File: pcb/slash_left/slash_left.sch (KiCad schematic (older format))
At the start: 76 parts

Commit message: pcb: slash: Matrix schematic
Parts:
- added D?: D_Small, symbol Device:D_Small
- added SW?: SW_Push_45deg, symbol Switch:SW_Push_45deg
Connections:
- net COL11: now also SW?.2
- net ROW0: now also D?.1 (K)
- new net: D?.2 (A), SW?.1
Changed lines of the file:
@@
 	5250 4600 6150 4600
 Wire Wire Line
-	6800 3650 6800 4900
+	6800 3650 6800 4200
 Wire Wire Line
-	6150 4600 7000 4600
+	6150 4600 6600 4600
+$Comp
+L Switch:SW_Push_45deg SW?
+U 1 1 61596B0E
+P 6700 4300
+F 0 "SW?" V 6600 4350 50  0000 R CNN
+F 1 "SW_Push_45deg" V 6655 4156 50  0001 R CNN
+F 2 "" H 6700 4300 50  0001 C CNN
+F 3 "~" H 6700 4300 50  0001 C CNN
+	1    6700 4300
+	0    -1   -1   0
+$EndComp
+$Comp
+L Device:D_Small D?
+U 1 1 615972C0
+P 6600 4500
+F 0 "D?" V 6600 4430 50  0000 R CNN
+F 1 "D_Small" V 6555 4430 50  0001 R CNN
+F 2 "" V 6600 4500 50  0001 C CNN
+F 3 "~" V 6600 4500 50  0001 C CNN
+	1    6600 4500
+	0    -1   -1   0
+$EndComp
+Connection ~ 6600 4600
+Wire Wire Line
+	6600 4600 7000 4600
+Connection ~ 6800 4200
+Wire Wire Line
+	6800 4200 6800 4900
 $EndSCHEMATC

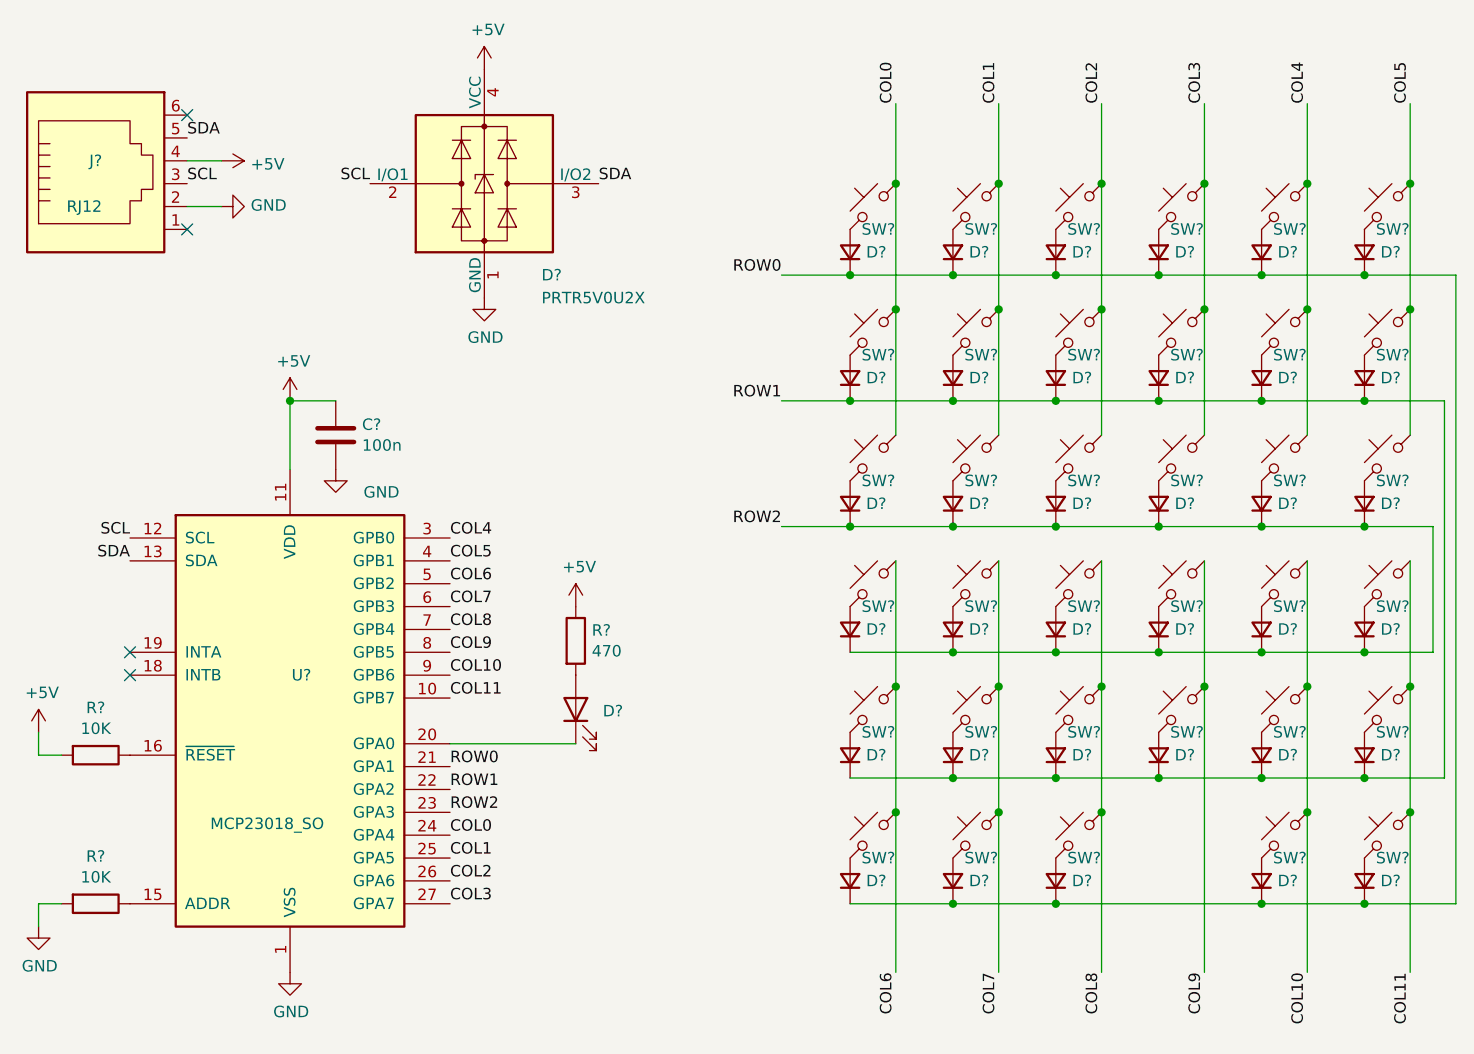
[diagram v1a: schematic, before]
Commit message: pcb: slash: left: Assign footprints
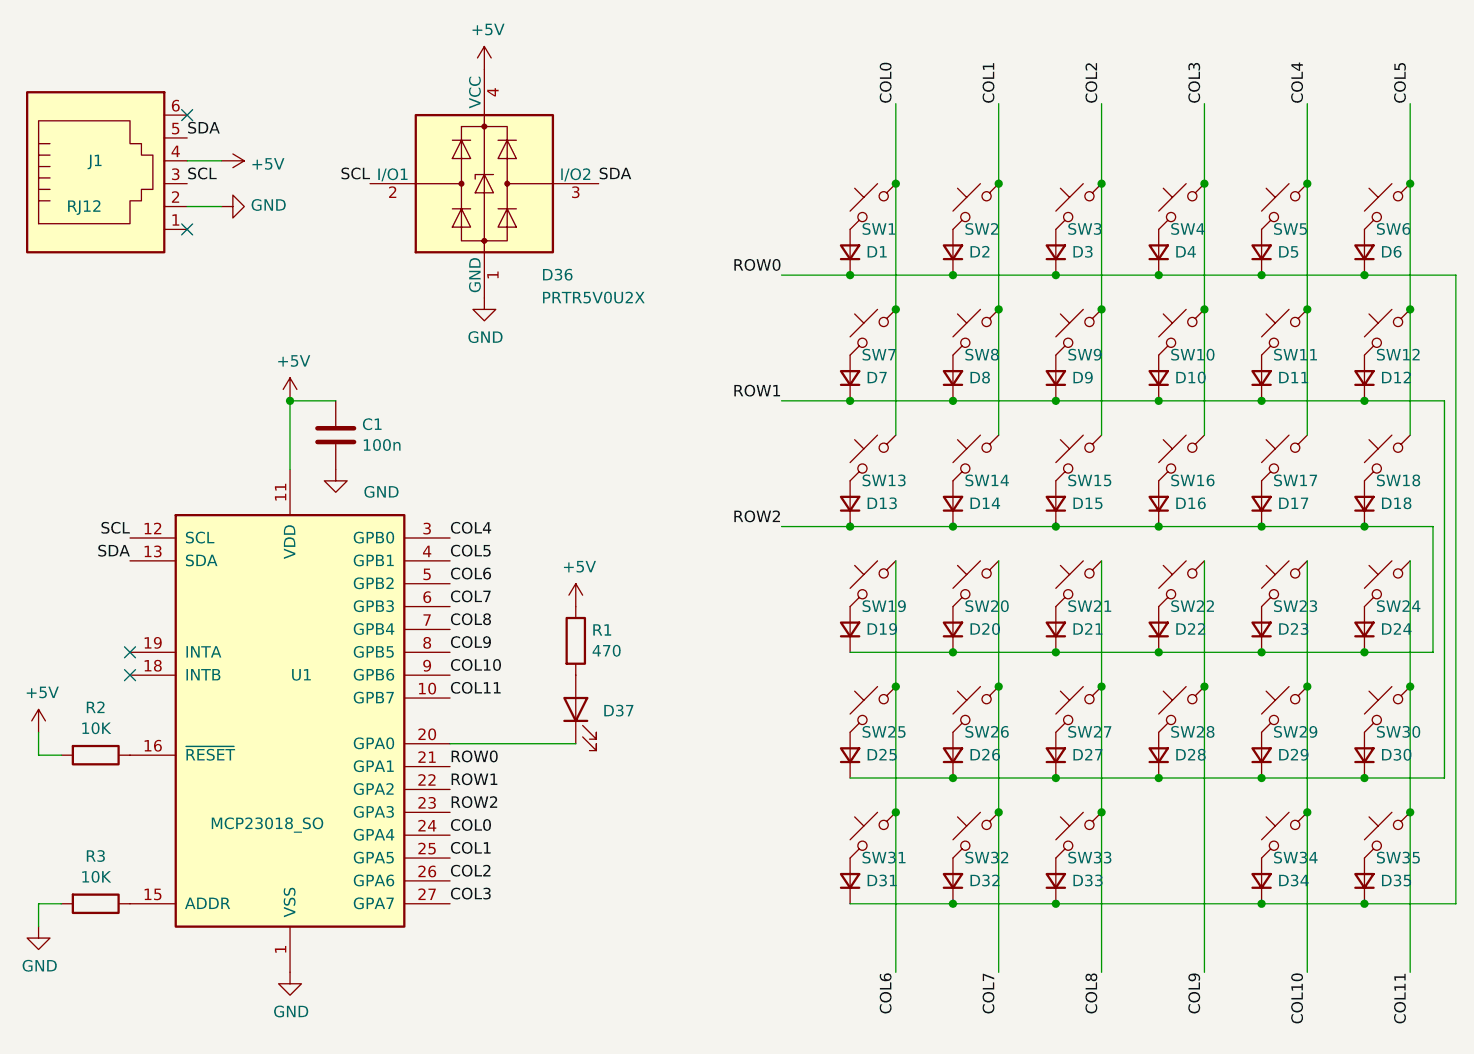
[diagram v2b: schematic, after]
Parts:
- C1: renamed from C?; footprint (none) -> Capacitor_SMD:C_0805_2012Metric_Pad1.18x1.45mm_HandSolder
- D1, D10, D11, D12, D13, D14, D15, D16, D17, D18, D19, D2, D20, D21, D22, D23, D24, D25, D26, D27, D28, D29, D3, D30, D31, D32, D33, D34, D35, D4, D5, D6, D7, D8, D9: renamed from D?; footprint (none) -> Diode_SMD:D_SOD-123
- D37: renamed from D?; footprint (none) -> LED_SMD:LED_0805_2012Metric_Pad1.15x1.40mm_HandSolder
- J1: renamed from J?; footprint (none) -> local_footprint:RJ12_Custom1
- R1, R2, R3: renamed from R?; footprint (none) -> Resistor_SMD:R_0805_2012Metric_Pad1.20x1.40mm_HandSolder
- SW1, SW10, SW11, SW12, SW13, SW14, SW15, SW16, SW17, SW18, SW19, SW2, SW20, SW21, SW22, SW23, SW24, SW25, SW26, SW27, SW28, SW29, SW3, SW30, SW31, SW32, SW33, SW34, SW35, SW4, SW5, SW6, SW7, SW8, SW9: renamed from SW?; footprint (none) -> keyswitches:Kailh_socket_MX
- gave numbers to parts that had none: 2

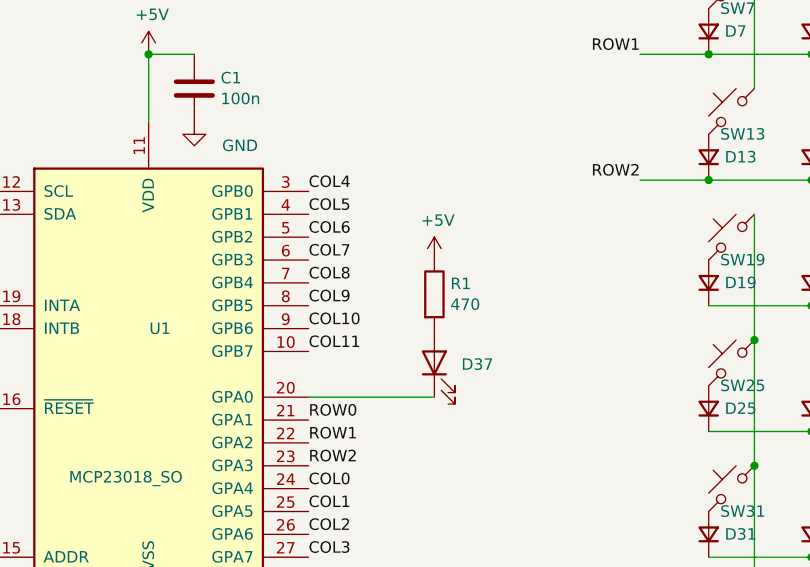
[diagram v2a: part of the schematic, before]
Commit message: pcb: slash: left: Routing
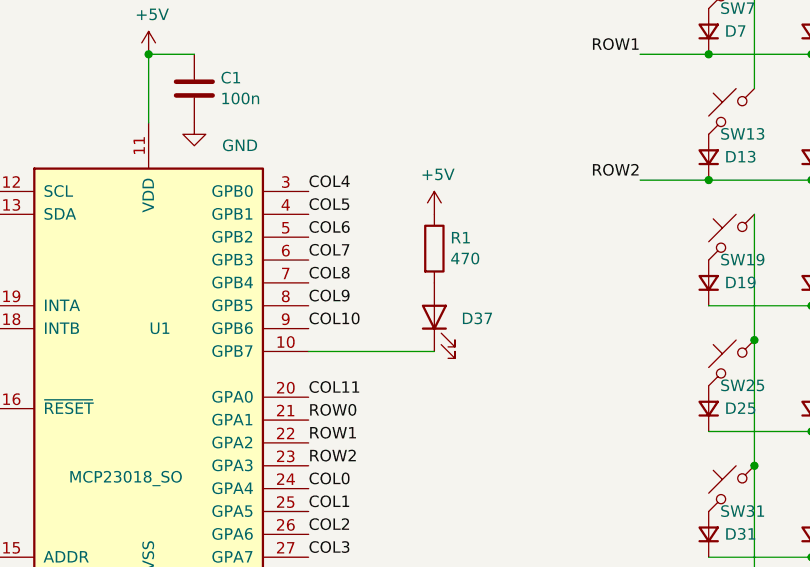
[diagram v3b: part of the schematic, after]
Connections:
- net COL11: now also U1.20 (GPA0); no longer U1.10 (GPB7)
- net at D37.1 (K): now also U1.10 (GPB7); no longer U1.20 (GPA0)
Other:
- moved on the sheet: D37, R1
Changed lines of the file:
@@
 L Device:LED D37
 U 1 1 6152B15D
-P 3150 3750
-F 0 "D37" V 3143 3632 50  0000 R CNN
-F 1 "LED" V 3098 3632 50  0001 R CNN
-F 2 "LED_SMD:LED_0805_2012Metric_Pad1.15x1.40mm_HandSolder" H 3150 3750 50  0001 C CNN
-F 3 "~" H 3150 3750 50  0001 C CNN
-	1    3150 3750
+P 3150 3550
+F 0 "D37" V 3143 3432 50  0000 R CNN
+F 1 "LED" V 3098 3432 50  0001 R CNN
+F 2 "LED_SMD:LED_0805_2012Metric_Pad1.15x1.40mm_HandSolder" H 3150 3550 50  0001 C CNN
+F 3 "~" H 3150 3550 50  0001 C CNN
+	1    3150 3550
 	0    -1   -1   0
 $EndComp
@@
 L Device:R R1
 U 1 1 6152D409
-P 3150 3450
-F 0 "R1" H 3220 3496 50  0000 L CNN
-F 1 "470" H 3220 3405 50  0000 L CNN
-F 2 "Resistor_SMD:R_0805_2012Metric_Pad1.20x1.40mm_HandSolder" V 3080 3450 50  0001 C CNN
-F 3 "~" H 3150 3450 50  0001 C CNN
-	1    3150 3450
+P 3150 3250
+F 0 "R1" H 3220 3296 50  0000 L CNN
+F 1 "470" H 3220 3205 50  0000 L CNN
+F 2 "Resistor_SMD:R_0805_2012Metric_Pad1.20x1.40mm_HandSolder" V 3080 3250 50  0001 C CNN
+F 3 "~" H 3150 3250 50  0001 C CNN
+	1    3150 3250
 	1    0    0    -1
 $EndComp
@@
 L power:+5V #PWR07
 U 1 1 6152E45E
-P 3150 3300
-F 0 "#PWR07" H 3150 3150 50  0001 C CNN
-F 1 "+5V" H 3165 3473 50  0000 C CNN
-F 2 "" H 3150 3300 50  0001 C CNN
-F 3 "" H 3150 3300 50  0001 C CNN
-	1    3150 3300
+P 3150 3100
+F 0 "#PWR07" H 3150 2950 50  0001 C CNN
+F 1 "+5V" H 3165 3273 50  0000 C CNN
+F 2 "" H 3150 3100 50  0001 C CNN
+F 3 "" H 3150 3100 50  0001 C CNN
+	1    3150 3100
 	1    0    0    -1
 $EndComp
 Wire Wire Line
-	3150 3900 2600 3900
+	3150 3700 2600 3700
 Text Label 2600 4000 0    50   ~ 0
 ROW0
@@
 Text Label 2600 3600 0    50   ~ 0
 COL10
-Text Label 2600 3700 0    50   ~ 0
+Text Label 2600 3900 0    50   ~ 0
 COL11
 Wire Wire Line

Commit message: pcb: slash: left: finish
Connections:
- net COL0: now also U1.6 (GPB3); no longer U1.24 (GPA4)
- net COL1: now also U1.7 (GPB4); no longer U1.25 (GPA5)
- net COL10: now also U1.22 (GPA2); no longer U1.9 (GPB6)
- net COL11: now also U1.21 (GPA1); no longer U1.20 (GPA0)
- net COL2: now also U1.8 (GPB5); no longer U1.26 (GPA6)
- net COL3: now also U1.9 (GPB6); no longer U1.27 (GPA7)
- net COL4: now also U1.27 (GPA7); no longer U1.3 (GPB0)
- net COL5: now also U1.20 (GPA0); no longer U1.4 (GPB1)
- net COL6: now also U1.26 (GPA6); no longer U1.5 (GPB2)
- net COL7: now also U1.25 (GPA5); no longer U1.6 (GPB3)
- net COL8: now also U1.24 (GPA4); no longer U1.7 (GPB4)
- net COL9: now also U1.23 (GPA3); no longer U1.8 (GPB5)
- net ROW0: now also U1.3 (GPB0); no longer U1.21 (GPA1)
- net ROW1: now also U1.4 (GPB1); no longer U1.22 (GPA2)
- net ROW2: now also U1.5 (GPB2); no longer U1.23 (GPA3)
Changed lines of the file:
@@
 Wire Wire Line
 	3150 3700 2600 3700
+Text Label 2600 3000 0    50   ~ 0
+ROW0
+Text Label 2600 3100 0    50   ~ 0
+ROW1
+Text Label 2600 3200 0    50   ~ 0
+ROW2
+Text Label 2600 3300 0    50   ~ 0
+COL0
+Text Label 2600 3400 0    50   ~ 0
+COL1
+Text Label 2600 3500 0    50   ~ 0
+COL2
+Text Label 2600 3600 0    50   ~ 0
+COL3
+Text Label 2600 4600 0    50   ~ 0
+COL4
+Text Label 2600 3900 0    50   ~ 0
+COL5
+Text Label 2600 4500 0    50   ~ 0
+COL6
+Text Label 2600 4400 0    50   ~ 0
+COL7
+Text Label 2600 4300 0    50   ~ 0
+COL8
+Text Label 2600 4200 0    50   ~ 0
+COL9
+Text Label 2600 4100 0    50   ~ 0
+COL10
 Text Label 2600 4000 0    50   ~ 0
-ROW0
-Text Label 2600 4100 0    50   ~ 0
-ROW1
-Text Label 2600 4200 0    50   ~ 0
-ROW2
-Text Label 2600 4300 0    50   ~ 0
-COL0
-Text Label 2600 4400 0    50   ~ 0
-COL1
-Text Label 2600 4500 0    50   ~ 0
-COL2
-Text Label 2600 4600 0    50   ~ 0
-COL3
-Text Label 2600 3000 0    50   ~ 0
-COL4
-Text Label 2600 3100 0    50   ~ 0
-COL5
-Text Label 2600 3200 0    50   ~ 0
-COL6
-Text Label 2600 3300 0    50   ~ 0
-COL7
-Text Label 2600 3400 0    50   ~ 0
-COL8
-Text Label 2600 3500 0    50   ~ 0
-COL9
-Text Label 2600 3600 0    50   ~ 0
-COL10
-Text Label 2600 3900 0    50   ~ 0
 COL11
 Wire Wire Line

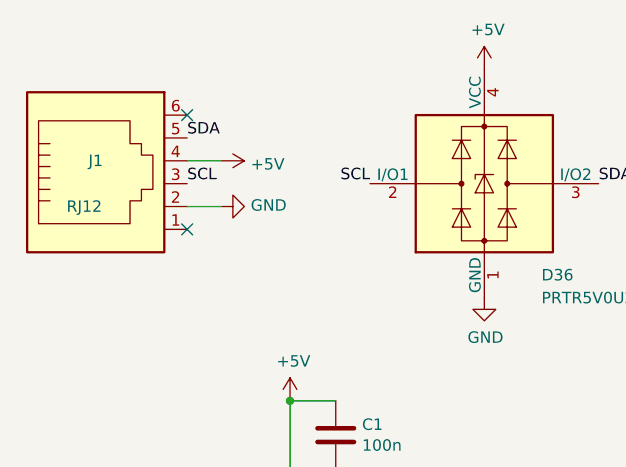
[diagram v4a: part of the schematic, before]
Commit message: pcb: slash: left: Add PWR flags
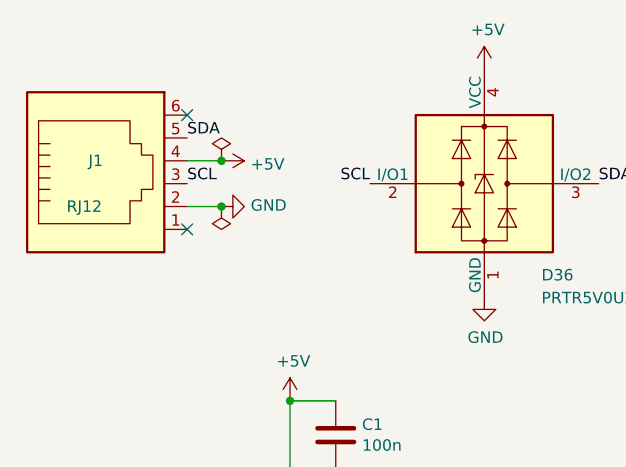
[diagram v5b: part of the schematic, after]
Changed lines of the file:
@@
 Wire Wire Line
 	6800 4200 6800 4900
+$Comp
+L power:PWR_FLAG #FLG0101
+U 1 1 61BFC6D4
+P 1600 1350
+F 0 "#FLG0101" H 1600 1425 50  0001 C CNN
+F 1 "PWR_FLAG" H 1850 1450 50  0001 C CNN
+F 2 "" H 1600 1350 50  0001 C CNN
+F 3 "~" H 1600 1350 50  0001 C CNN
+	1    1600 1350
+	1    0    0    -1
+$EndComp
+Connection ~ 1600 1350
+$Comp
+L power:PWR_FLAG #FLG0102
+U 1 1 61C044DF
+P 1600 1550
+F 0 "#FLG0102" H 1600 1625 50  0001 C CNN
+F 1 "PWR_FLAG" H 1350 1700 50  0001 C CNN
+F 2 "" H 1600 1550 50  0001 C CNN
+F 3 "~" H 1600 1550 50  0001 C CNN
+	1    1600 1550
+	-1   0    0    1
+$EndComp
+Connection ~ 1600 1550
 $EndSCHEMATC
